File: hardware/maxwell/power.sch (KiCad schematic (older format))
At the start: 53 parts, among them J7 Dynamo Input, J9 Battery, Q2 PSMN5R4-25YLD, Q3 DMG9926UDM, Q4 NTR1P02T1, Q5 NTR1P02T1, U1 MCP1501, U10 MIC39102, U11 AP9101C-SOT-25, U12 INA219AID, U13 PCF8593, U3 TPS2113, U4 PCA9536D, U6 AD7991, U8 TLP188, U9 Buck Regulator

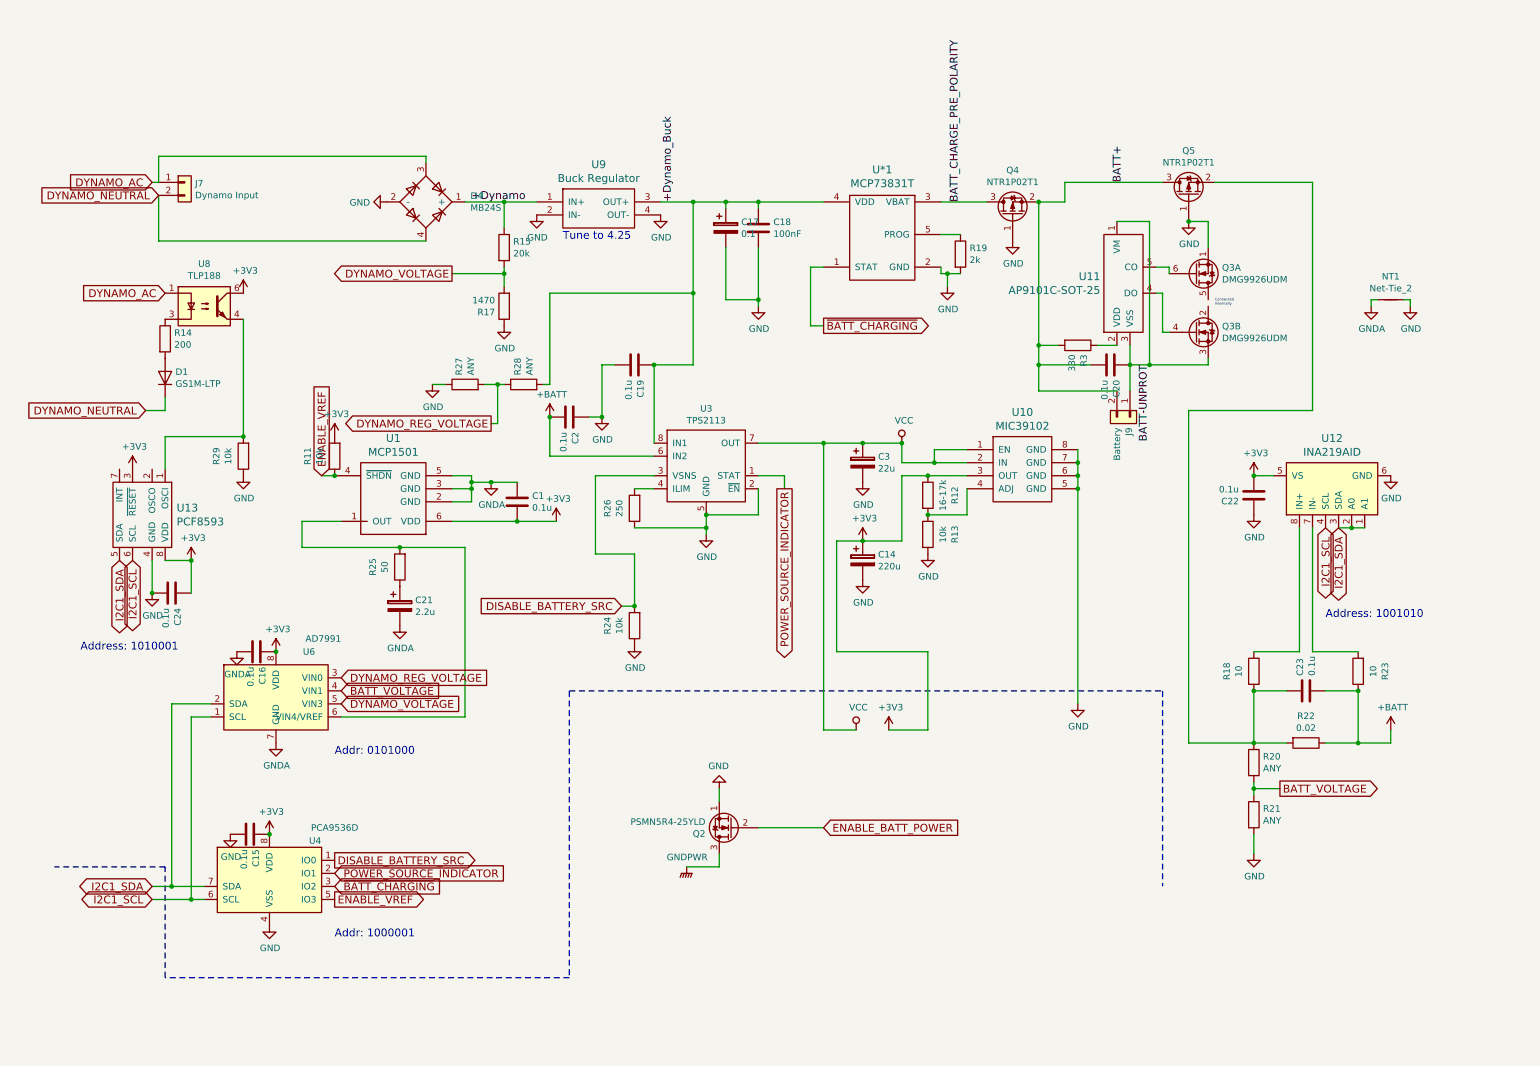
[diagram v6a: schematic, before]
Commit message: Revision 1.9a
* Separates PCB into three boards (from two); adding a new
  'Rectifier' board mounted directly to the 'Power' board via a
  board-to-board connector.
* Switches to active rectification.
* Provide 5V directly to the battery; drop VCC voltage to
  4.3V via a diode drop.
* Adds new WAKE-controlled power switch to reduce quiescent
  current to, essentially, nil, and remove the need
  carefully managing sleep states of various devices.
* Adds 220uF capacitor to 3V3 output on 'Main' PCB.
* Control power to SPI/I2C connector via a new uC-controlled MOSFET.
* Adds clock chip to main uC board for permanent timekeeping and
  alarm-based wakeup.
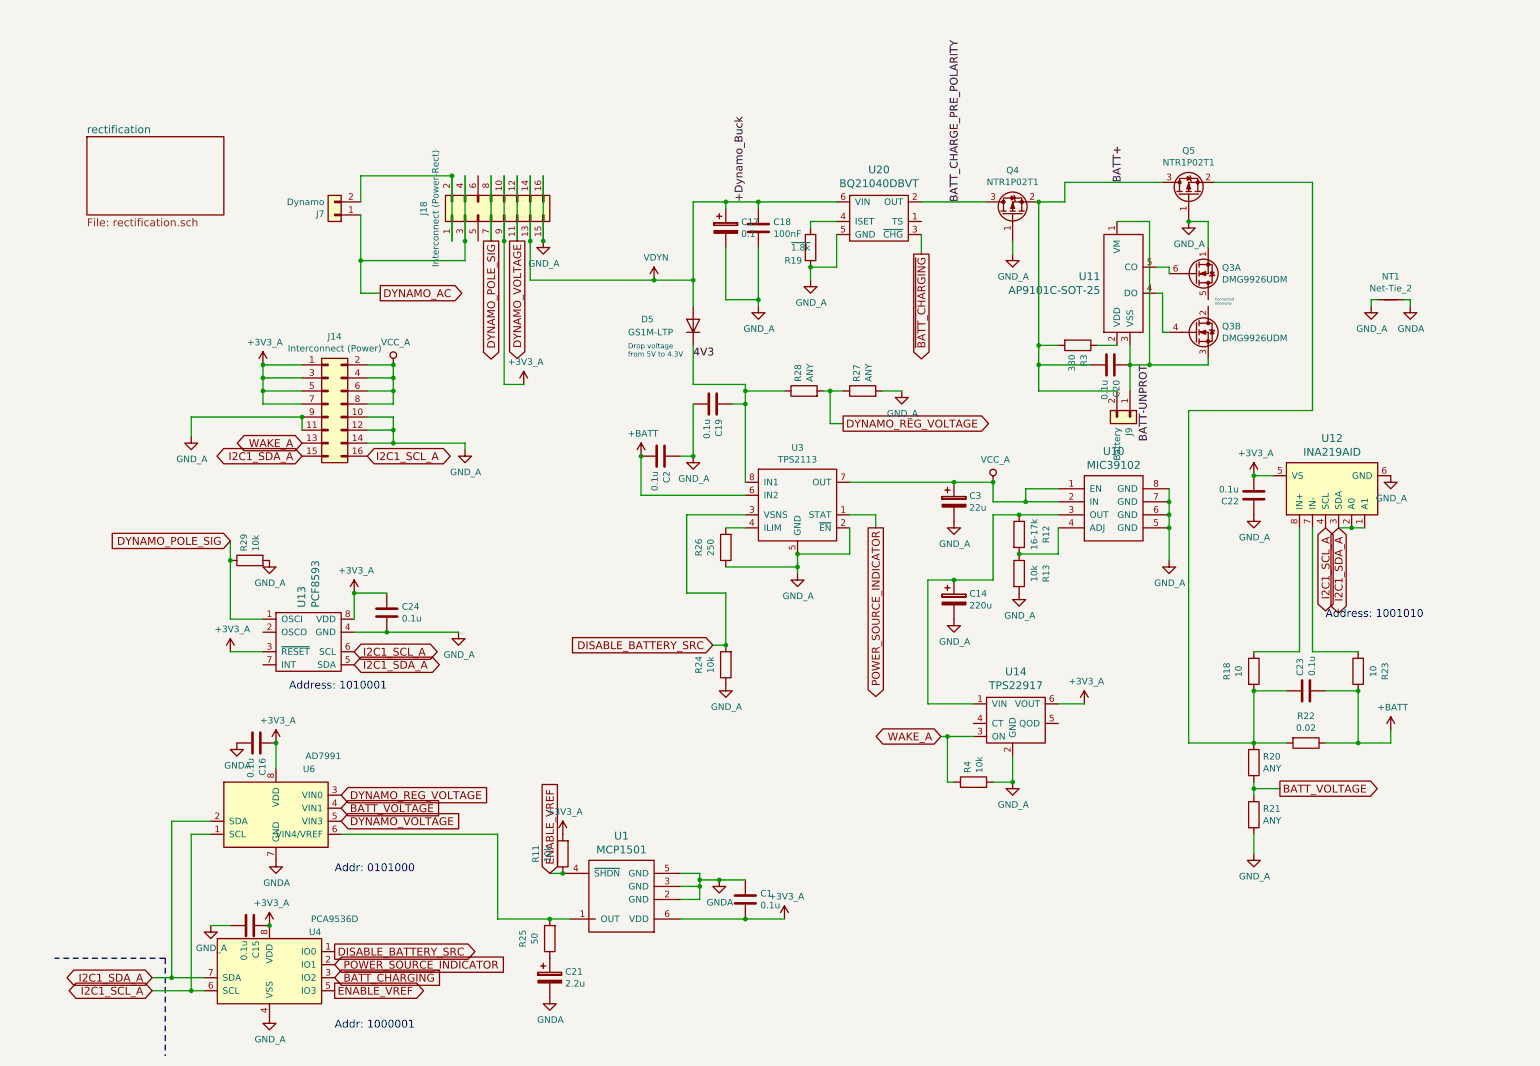
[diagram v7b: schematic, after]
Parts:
- removed D1: GS1M-LTP, coddingtonbear:DO-214AC, symbol maxwell-rescue:D-RESCUE-maxwell
- removed D4: MB24S, coddingtonbear:SO-4_Milling, symbol maxwell-rescue:D_Bridge_+-AA-RESCUE-maxwell
- removed Q2: PSMN5R4-25YLD, coddingtonbear:PSMN5R4-25YLD, symbol maxwell-rescue:Q_NMOS_SGD-device
- removed R14: 200, coddingtonbear:0805_Milling, symbol maxwell-rescue:R-RESCUE-maxwell
- removed R15: 20k, coddingtonbear:0805_Milling, symbol maxwell-rescue:R-RESCUE-maxwell
- removed R17: 1470, coddingtonbear:0805_Milling, symbol maxwell-rescue:R-RESCUE-maxwell
- removed U*1: MCP73831T, Package_TO_SOT_SMD:SOT-23-5_HandSoldering, symbol maxwell-rescue:MCP73831T-RESCUE-maxwell
- removed U8: TLP188, coddingtonbear:SO-4_Optocoupler_Milling, symbol maxwell-rescue:TLP185(SE-RESCUE-maxwell
- removed U9: Buck Regulator, coddingtonbear:BOOST_LM2596_3A, symbol maxwell-rescue:BOOST_BOARD-RESCUE-maxwell
- added D5: GS1M-LTP, coddingtonbear:D_SOD-123_LargePads, symbol Device:D
- added J14: Interconnect (Power), coddingtonbear:IDC-Header_2x08_P2.54mm_Vertical_Largepads, symbol Connector_Generic:Conn_02x08_Odd_Even
- added J18: Interconnect (Power-Rect), coddingtonbear:PinHeader_2x08_P2.54mm_Vertical_LargePads, symbol Connector_Generic:Conn_02x08_Odd_Even
- added R4: 10k, coddingtonbear:0805_Milling, symbol maxwell-rescue:R-RESCUE-maxwell
- added U14: TPS22917, Package_TO_SOT_SMD:SOT-23-6_Handsoldering, symbol coddingtonbear:TPS22917
- added U20: BQ21040DBVT, Package_TO_SOT_SMD:SOT-23-6_Handsoldering, symbol coddingtonbear:BQ21040DBVT
- J7: value Dynamo Input -> Dynamo
- R19: value 2k -> ~1.8k
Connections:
- net BATT_CHARGE_PRE_POLARITY: now also U20.2 (OUT)
- net DYNAMO_AC: now also J18.3 (Pin_3), J18.4 (Pin_4)
- net DYNAMO_REG_VOLTAGE: now also R27.1, R28.2; no longer R27.2, R28.1
- net DYNAMO_VOLTAGE: now also J18.11 (Pin_11), J18.12 (Pin_12)
- net GNDA: now also NT1.2; no longer NT1.1
- net ~BATT_CHARGING: now also U20.3 (~CHG)
- net DYNAMO_POLE_SIG: now reaches U13.1 (OSCI)
- net DYNAMO_POLE_SIG: now also R29.1, J18.7 (Pin_7), J18.8 (Pin_8); no longer R29.2
- net at R19.1: now also U20.4 (ISET)
- net +3V3 renamed +3V3_A
- net +3V3_A: now also J14.1 (Pin_1), J14.3 (Pin_3), J14.5 (Pin_5), J14.7 (Pin_7), J18.10 (Pin_10), J18.9 (Pin_9), U14.6 (VOUT); no longer C14.1, R12.1, U10.3 (OUT)
- removed net +Dynamo_Buck: C17.1, C18.2, C19.2, R28.2, U3.8 (IN1)
- net DYNAMO_NEUTRAL: no longer names the net of J7.2 (Pin_2)
- net DYNAMO_NEUTRAL: now also J18.1 (Pin_1), J18.2 (Pin_2)
- net GND renamed GND_A
- net GND_A: now also NT1.1, R27.2, R29.2, J14.10 (Pin_10), J14.11 (Pin_11), J14.12 (Pin_12), J14.14 (Pin_14), J14.9 (Pin_9), J18.15 (Pin_15), J18.16 (Pin_16), R4.2, U14.2 (GND), U20.5 (GND); no longer NT1.2, R27.1, R29.1
- net I2C1_SCL renamed I2C1_SCL_A
- net I2C1_SCL_A: now also J14.16 (Pin_16)
- net I2C1_SDA renamed I2C1_SDA_A
- net I2C1_SDA_A: now also J14.15 (Pin_15)
- net VCC renamed VCC_A
- net VCC_A: now also J14.2 (Pin_2), J14.4 (Pin_4), J14.6 (Pin_6), J14.8 (Pin_8)
- new net: C14.1, R12.1, U10.3 (OUT), U14.1 (VIN)
- new net 4V3: C19.2, D5.1 (K), R28.1, U3.8 (IN1)
- new net VDYN: C17.1, C18.2, D5.2 (A), J18.13 (Pin_13), J18.14 (Pin_14), U20.6 (VIN)
- new net WAKE_A: J14.13 (Pin_13), R4.1, U14.3 (ON)
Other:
- note added: "Drop voltage\nfrom 5V to 4.3V"
- note removed: "Tune to 4.25"
- moved on the sheet: C1, C14, C15, C16, C19, C2, C21, C24, C3, R11, R12, R13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

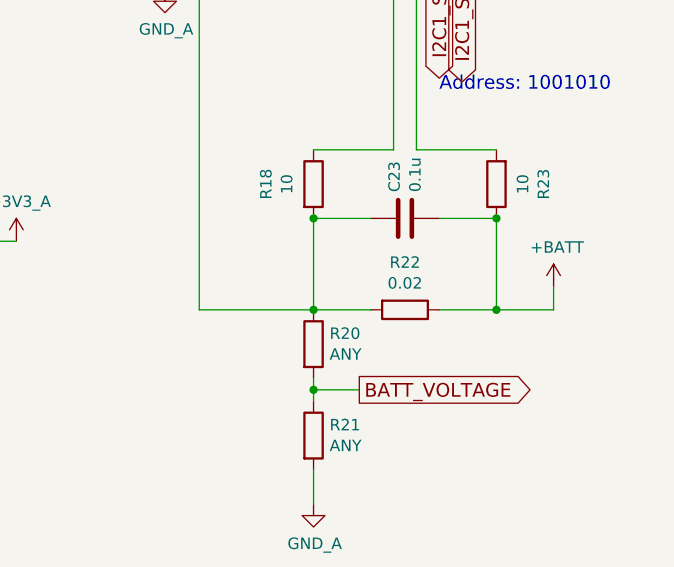
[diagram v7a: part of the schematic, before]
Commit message: Fixing errata:
* Connecting ESP32 to WAKE to ensure that the ESP32 can keep
  the power on while doing things like flashing the uC.
* Pull power button high to VCC via a diode instead of
  3V3 which is the very thing the power button will be
  turning on.
* Updating sense resistor to 100mOhm instead of 20mOhm.
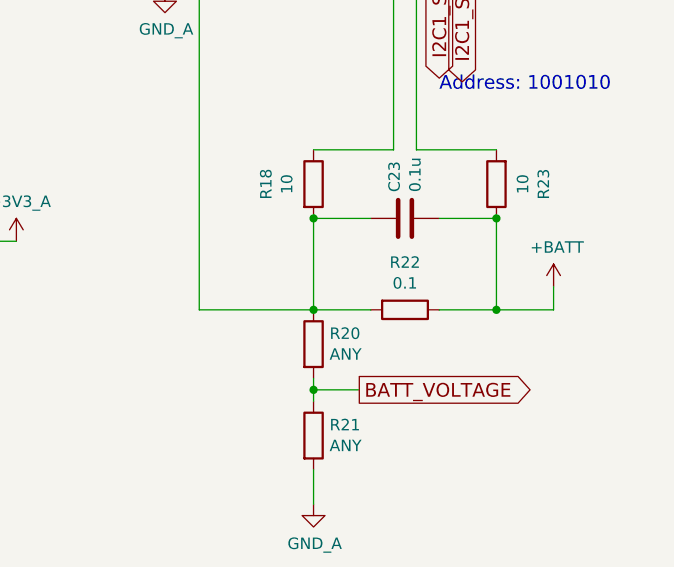
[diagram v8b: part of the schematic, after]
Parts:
- R22: value 0.02 -> 0.1
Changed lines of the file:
@@
 P 10100 5400
 F 0 "R22" V 9893 5400 50  0000 C CNN
-F 1 "0.02" V 9984 5400 50  0000 C CNN
+F 1 "0.1" V 9984 5400 50  0000 C CNN
 F 2 "coddingtonbear:0805_Milling" V 10030 5400 50  0001 C CNN
 F 3 "" H 10100 5400 50  0001 C CNN
